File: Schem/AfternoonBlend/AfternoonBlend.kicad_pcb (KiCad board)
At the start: 4 copper layers, 160 x 64.4 mm, 67 parts, among them J1 pBITzBus, J4 STX-3120-3B, J5 Conn_01x03, SW1 SW_Coded_SH-7070, U1 74HC688, U10 LM4880MX/NOPB, U11 SN76489AN, U12 SN76489AN, U2 TLV2372, U3 AD7801BRUZ, U6 SN76489AN, U7 SN76489AN, U8 74HC138, U9 74HCT21, Y1 ECS-2100A-035

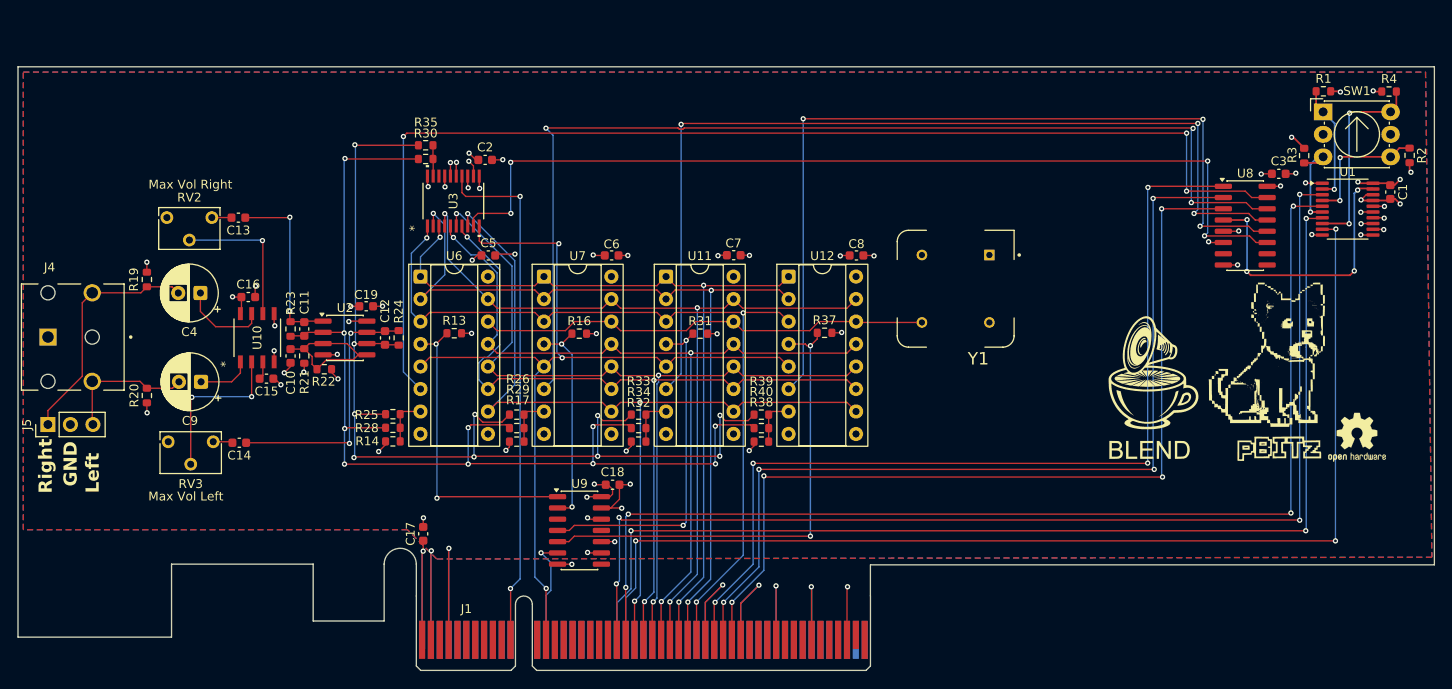
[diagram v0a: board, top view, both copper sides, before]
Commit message: Added a buffer on the Data Line to avoid overloading the CPU data bus with the 5 ICs on the board.
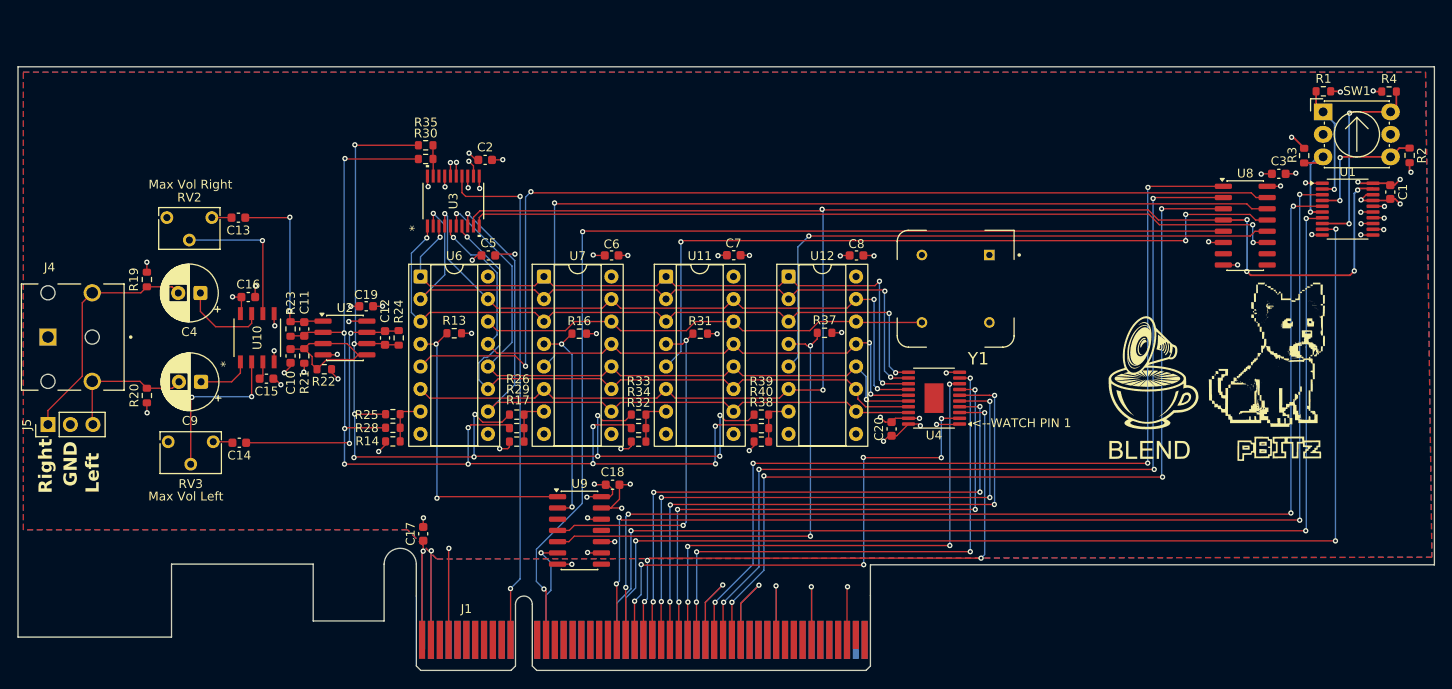
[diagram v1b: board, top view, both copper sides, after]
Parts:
- removed REF**: OSHW-Logo2_7.3x6mm_SilkScreen, Symbol:OSHW-Logo2_7.3x6mm_SilkScreen
- added C20: 100n, Capacitor_SMD:C_0603_1608Metric, F.Cu at (162.5, 104.7)
- added U4: 74HCT541, Package_SO:TSSOP-20-1EP_4.4x6.5mm_P0.65mm_EP2.15x3.35mm, F.Cu at (167.3, 101.2)
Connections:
- J1 pad B23: /Sound/D0 -> /pBITz Bus Interface/D0
- J1 pad B24: /Sound/D1 -> /pBITz Bus Interface/D1
- J1 pad B25: /Sound/D2 -> /pBITz Bus Interface/D2
- J1 pad B26: /Sound/D3 -> /pBITz Bus Interface/D3
- J1 pad B27: /Sound/D4 -> /pBITz Bus Interface/D4
- J1 pad B28: /Sound/D5 -> /pBITz Bus Interface/D5
- J1 pad B29: /Sound/D6 -> /pBITz Bus Interface/D6
- J1 pad B30: /Sound/D7 -> /pBITz Bus Interface/D7
- U11 pad 1: /Sound/D5 -> /Sound/DB5
- U11 pad 10: /Sound/D0 -> /Sound/DB0
- U11 pad 11: /Sound/D1 -> /Sound/DB1
- U11 pad 12: /Sound/D2 -> /Sound/DB2
- U11 pad 13: /Sound/D3 -> /Sound/DB3
- U11 pad 15: /Sound/D4 -> /Sound/DB4
- U11 pad 2: /Sound/D6 -> /Sound/DB6
- U11 pad 3: /Sound/D7 -> /Sound/DB7
- U11 pad 5: /Sound/~{WR} -> /Sound/~{PSG2}
- U11 pad 6: /Sound/~{PSG2} -> /Device Select Decode/~{CS_SOUND}
- U12 pad 1: /Sound/D5 -> /Sound/DB5
- U12 pad 10: /Sound/D0 -> /Sound/DB0
- U12 pad 11: /Sound/D1 -> /Sound/DB1
- U12 pad 12: /Sound/D2 -> /Sound/DB2
- U12 pad 13: /Sound/D3 -> /Sound/DB3
- U12 pad 15: /Sound/D4 -> /Sound/DB4
- U12 pad 2: /Sound/D6 -> /Sound/DB6
- U12 pad 3: /Sound/D7 -> /Sound/DB7
- U12 pad 5: /Sound/~{WR} -> /Sound/~{PSG3}
- U12 pad 6: /Sound/~{PSG3} -> /Device Select Decode/~{CS_SOUND}
- U3 pad 1: /Sound/D7 -> /Sound/DB7
- U3 pad 10: /Sound/~{WR} -> /Sound/~{PCM}
- U3 pad 2: /Sound/D6 -> /Sound/DB6
- U3 pad 3: /Sound/D5 -> /Sound/DB5
- U3 pad 4: /Sound/D4 -> /Sound/DB4
- U3 pad 5: /Sound/D3 -> /Sound/DB3
- U3 pad 6: /Sound/D2 -> /Sound/DB2
- U3 pad 7: /Sound/D1 -> /Sound/DB1
- U3 pad 8: /Sound/D0 -> /Sound/DB0
- U3 pad 9: /Sound/~{PCM} -> /Device Select Decode/~{CS_SOUND}
- U6 pad 1: /Sound/D5 -> /Sound/DB5
- U6 pad 10: /Sound/D0 -> /Sound/DB0
- U6 pad 11: /Sound/D1 -> /Sound/DB1
- U6 pad 12: /Sound/D2 -> /Sound/DB2
- U6 pad 13: /Sound/D3 -> /Sound/DB3
- U6 pad 15: /Sound/D4 -> /Sound/DB4
- U6 pad 2: /Sound/D6 -> /Sound/DB6
- U6 pad 3: /Sound/D7 -> /Sound/DB7
- U6 pad 5: /Sound/~{WR} -> /Sound/~{PSG0}
- U6 pad 6: /Sound/~{PSG0} -> /Device Select Decode/~{CS_SOUND}
- U7 pad 1: /Sound/D5 -> /Sound/DB5
- U7 pad 10: /Sound/D0 -> /Sound/DB0
- U7 pad 11: /Sound/D1 -> /Sound/DB1
- U7 pad 12: /Sound/D2 -> /Sound/DB2
- U7 pad 13: /Sound/D3 -> /Sound/DB3
- U7 pad 15: /Sound/D4 -> /Sound/DB4
- U7 pad 2: /Sound/D6 -> /Sound/DB6
- U7 pad 3: /Sound/D7 -> /Sound/DB7
- U7 pad 5: /Sound/~{WR} -> /Sound/~{PSG1}
- U7 pad 6: /Sound/~{PSG1} -> /Device Select Decode/~{CS_SOUND}
- U8 pad 5: GND -> /Sound/~{WR}
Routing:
- net /Device Select Decode/~{CS_SOUND}: track 32.2 -> 187.3 mm, vias 4 -> 6
- net /Sound/D0: track 98.5 -> 0.00 mm, vias 3 -> 0
- net /Sound/D6: track 97.5 -> 0.00 mm, vias 3 -> 0
- net /Sound/D2: track 96.9 -> 0.00 mm, vias 3 -> 0
- net /Sound/D4: track 96.0 -> 0.00 mm, vias 3 -> 0
- net /Sound/D1: track 95.9 -> 0.00 mm, vias 3 -> 0
- net /Sound/D7: track 95.2 -> 0.00 mm, vias 3 -> 0
- net /Sound/D3: track 94.5 -> 0.00 mm, vias 3 -> 0
- net /Sound/D5: track 92.0 -> 0.00 mm, vias 3 -> 0
- net /Sound/DB6: track 0.00 -> 80.0 mm, vias 0 -> 3
- net /Sound/DB0: track 0.00 -> 77.0 mm, vias 0 -> 1
- net /Sound/DB7: track 0.00 -> 76.1 mm, vias 0 -> 3
- net /Sound/DB5: track 0.00 -> 76.0 mm, vias 0 -> 3
- net /Sound/DB2: track 0.00 -> 75.8 mm, vias 0 -> 2
- net /Sound/DB1: track 0.00 -> 73.0 mm, vias 0 -> 1
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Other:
- board text added: "<--WATCH PIN 1"

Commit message: Put back /CS_SOUND as the qualifying signal instead of /WR
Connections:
- U11 pad 5: /Sound/~{PSG2} -> /Sound/~{WR}
- U11 pad 6: /Device Select Decode/~{CS_SOUND} -> /Sound/~{PSG2}
- U12 pad 5: /Sound/~{PSG3} -> /Sound/~{WR}
- U12 pad 6: /Device Select Decode/~{CS_SOUND} -> /Sound/~{PSG3}
- U3 pad 10: /Sound/~{PCM} -> /Sound/~{WR}
- U3 pad 9: /Device Select Decode/~{CS_SOUND} -> /Sound/~{PCM}
- U6 pad 5: /Sound/~{PSG0} -> /Sound/~{WR}
- U6 pad 6: /Device Select Decode/~{CS_SOUND} -> /Sound/~{PSG0}
- U7 pad 5: /Sound/~{PSG1} -> /Sound/~{WR}
- U7 pad 6: /Device Select Decode/~{CS_SOUND} -> /Sound/~{PSG1}
- U8 pad 5: /Sound/~{WR} -> GND
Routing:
- net /Device Select Decode/~{CS_SOUND}: track 187.3 -> 32.2 mm, vias 6 -> 4
- net /Sound/~{WR}: track 121.1 -> 95.0 mm
- net /Sound/~{PCM}: track 92.6 -> 95.4 mm
- net /Sound/~{PSG3}: track 67.7 -> 70.2 mm
- net /Sound/~{PSG2}: track 84.3 -> 86.8 mm
- net /Sound/~{PSG1}: track 99.7 -> 102.3 mm
- net GND: track 152.4 -> 154.0 mm, vias 52 -> 53
- net /Sound/~{PSG0}: track 116.3 -> 117.3 mm

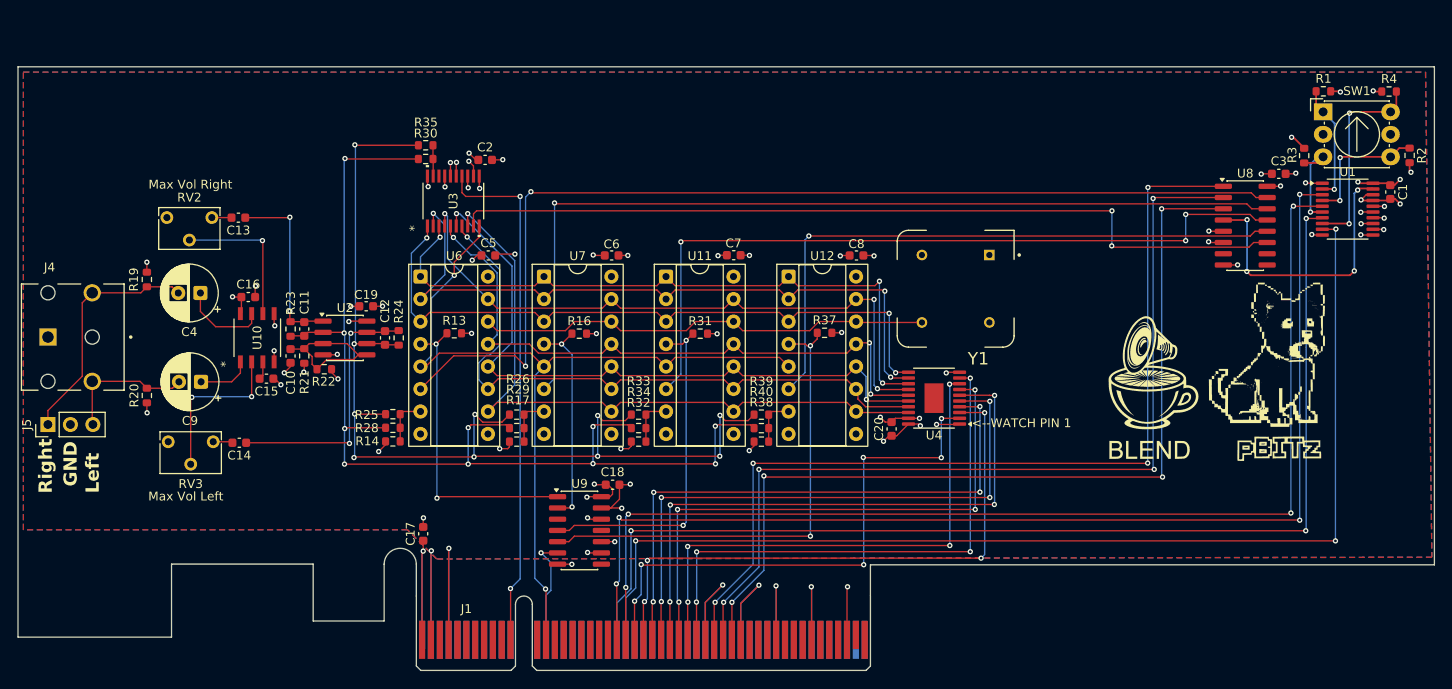
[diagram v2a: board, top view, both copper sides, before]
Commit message: Added wait-state generation to cope with a 10MHz cpu
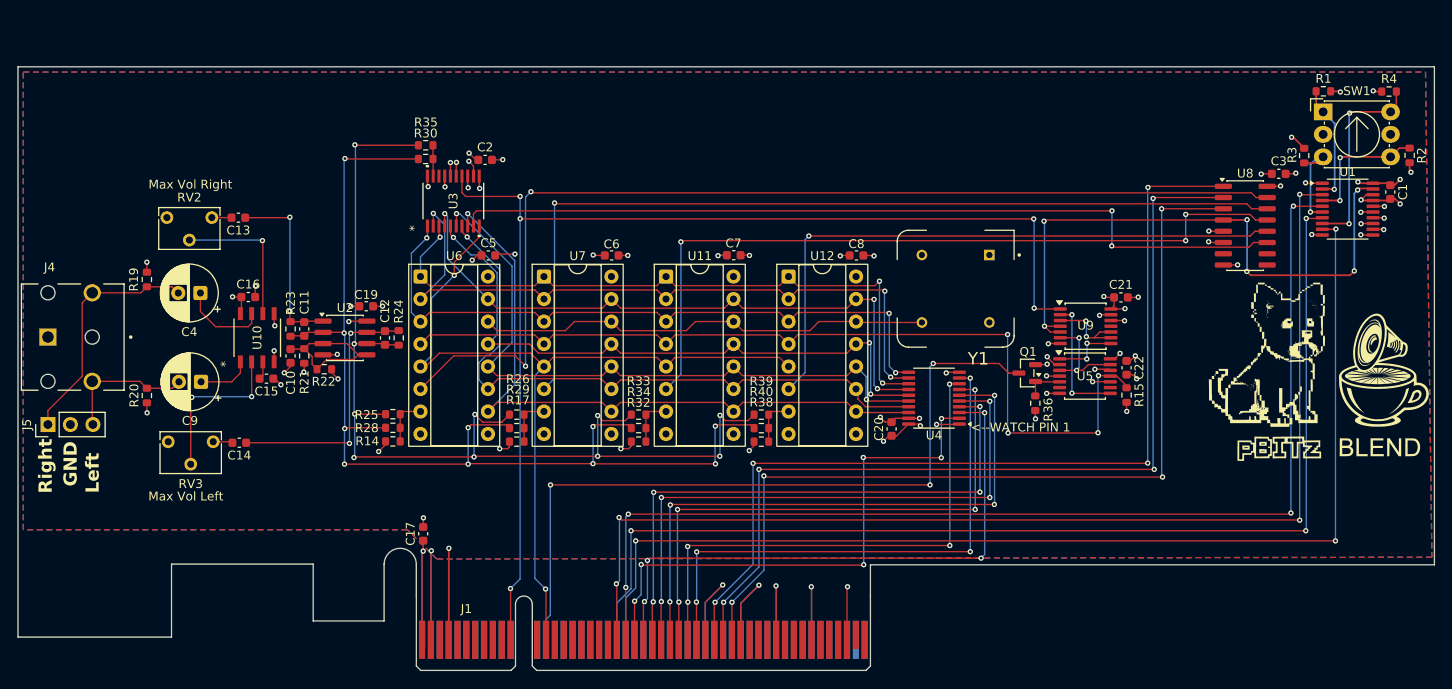
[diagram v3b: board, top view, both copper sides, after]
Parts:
- removed C18: 100n, Capacitor_SMD:C_0603_1608Metric
- removed R13, R16, R31, R37: 10k, Resistor_SMD:R_0603_1608Metric
- added C21: 100n, Capacitor_SMD:C_0603_1608Metric, F.Cu at (188.4, 89.8)
- added C22: 100n, Capacitor_SMD:C_0603_1608Metric, F.Cu at (189.0, 97.8)
- added Q1: 2N7002, Package_TO_SOT_SMD:SOT-23, F.Cu at (177.8, 98.4)
- added R15: 10k, Resistor_SMD:R_0603_1608Metric, F.Cu at (189.0, 100.9)
- added R36: 47k, Resistor_SMD:R_0603_1608Metric, F.Cu at (178.7, 101.8)
- added U5: 74AHCT74, Package_SO:TSSOP-14_4.4x5mm_P0.65mm, F.Cu at (184.3, 98.7)
- U4: footprint Package_SO:TSSOP-20-1EP_4.4x6.5mm_P0.65mm_EP2.15x3.35mm -> Package_SO:TSSOP-20_4.4x6.5mm_P0.65mm
- U9: value 74HCT21 -> 74AHCT00; footprint Package_SO:SOIC-14_3.9x8.7mm_P1.27mm -> Package_SO:TSSOP-14_4.4x5mm_P0.65mm
- moved U9 61.6 mm to (184.4, 93.1)
- moved G*** 26.0 mm to (217.6, 99.3)
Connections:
- U11 pad 4: /Sound/READY2 -> /Sound/READY_ALL
- U12 pad 4: /Sound/READY3 -> /Sound/READY_ALL
- U6 pad 4: /Sound/READY0 -> /Sound/READY_ALL
- U7 pad 4: /Sound/READY1 -> /Sound/READY_ALL
- U9 pad 1: /Sound/READY0 -> /Sound/~{RESET}
- U9 pad 10: GND -> /Sound/FF2_CLR
- U9 pad 11: (no net) -> unconnected-(U9-Pad11)
- U9 pad 2: /Sound/READY1 -> /Sound/~{FF2_Q}
- U9 pad 3: (no net) -> /Sound/FF2_CLR
- U9 pad 4: /Sound/READY2 -> /Device Select Decode/~{CS_SOUND}
- U9 pad 5: /Sound/READY3 -> /Device Select Decode/~{CS_SOUND}
- U9 pad 6: /Sound/~{WAIT} -> /Sound/CS_SOUND
- U9 pad 8: unconnected-(U9-Pad8) -> /Sound/~{FF2_CLR}
- U9 pad 9: GND -> /Sound/FF2_CLR
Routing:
- net /Sound/READY_ALL: track 0.00 -> 101.0 mm, vias 0 -> 4
- net /Sound/~{WAIT}: track 12.4 -> 84.6 mm, vias 1 -> 3
- net /Sound/~{RESET}: track 59.2 -> 130.3 mm, vias 2 -> 5
- net /Sound/READY3: track 54.7 -> 0.00 mm, vias 2 -> 0
- net /Sound/READY2: track 39.0 -> 0.00 mm, vias 2 -> 0
- net /Device Select Decode/~{CS_SOUND}: track 32.2 -> 68.3 mm, vias 4 -> 6
- net /Sound/READY0: track 34.6 -> 0.00 mm, vias 2 -> 0
- net /Sound/READY1: track 24.2 -> 0.00 mm, vias 2 -> 0
- net /Sound/~{FF2_Q}: track 0.00 -> 14.5 mm, vias 0 -> 2
- net /Sound/CS_SOUND: track 0.00 -> 11.9 mm, vias 0 -> 2
- net /Sound/FF2_CLR: track 0.00 -> 9.70 mm, vias 0 -> 2
- net /Sound/~{FF2_CLR}: track 0.00 -> 7.58 mm, vias 0 -> 2
- net +5V: track 90.2 -> 94.8 mm, vias 31 -> 34
- net /Sound/WAIT_GATE: track 0.00 -> 4.39 mm
- net GND: track 154.0 -> 151.6 mm, vias 53 -> 55

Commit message: Added WS Generator to sound card to match the speed of the CPU to the speed of the SN7 chips
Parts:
- added C23: 100n, Capacitor_SMD:C_0603_1608Metric, F.Cu at (202.2, 90.0)
- added U14: 74AHC20, Package_SO:TSSOP-14_4.4x5mm_P0.65mm, F.Cu at (198.1, 93.3)
- R15: value 10k -> 2k2
- moved G*** 2.18 mm to (208.4, 96.9)
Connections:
- U8 pad 5: GND -> /Sound/~{WR}
- U9 pad 4: /Device Select Decode/~{CS_SOUND} -> GND
- U9 pad 5: /Device Select Decode/~{CS_SOUND} -> GND
- U9 pad 6: /Sound/CS_SOUND -> unconnected-(U9-Pad6)
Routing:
- net /Sound/~{WR}: track 95.0 -> 158.8 mm, vias 2 -> 4
- net /Device Select Decode/~{CS_SOUND}: track 68.3 -> 32.2 mm, vias 6 -> 4
- net /Sound/~{PSG0}: track 117.3 -> 133.0 mm, vias 2 -> 4
- net /Sound/~{PSG1}: track 102.3 -> 116.2 mm, vias 1 -> 3
- net /Sound/~{PSG3}: track 70.2 -> 83.1 mm, vias 1 -> 3
- net /Sound/~{PSG2}: track 86.8 -> 98.4 mm, vias 3 -> 4
- net GND: track 151.6 -> 161.1 mm, vias 55 -> 62
- net +5V: track 94.8 -> 100.2 mm, vias 34 -> 36
- net /Sound/CS_SOUND: track 11.9 -> 17.3 mm

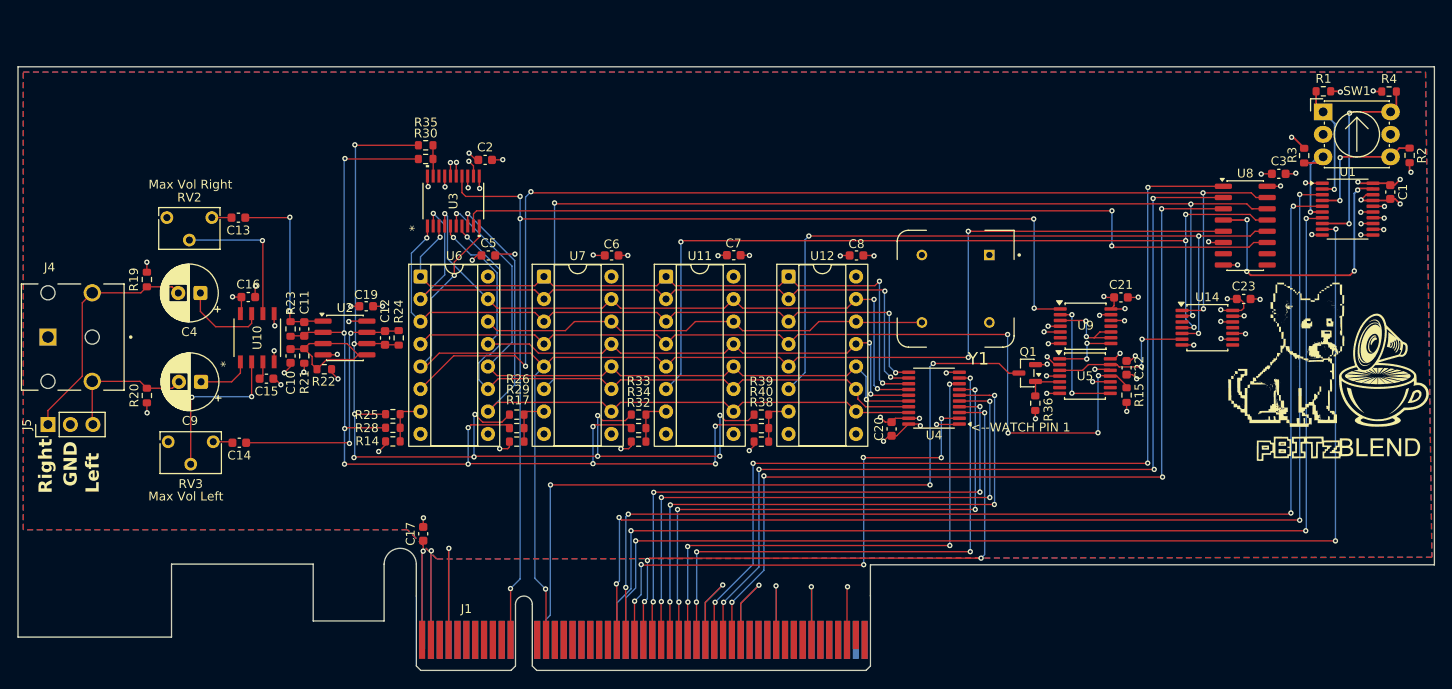
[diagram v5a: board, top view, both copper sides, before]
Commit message: Moved to the DIN Connector
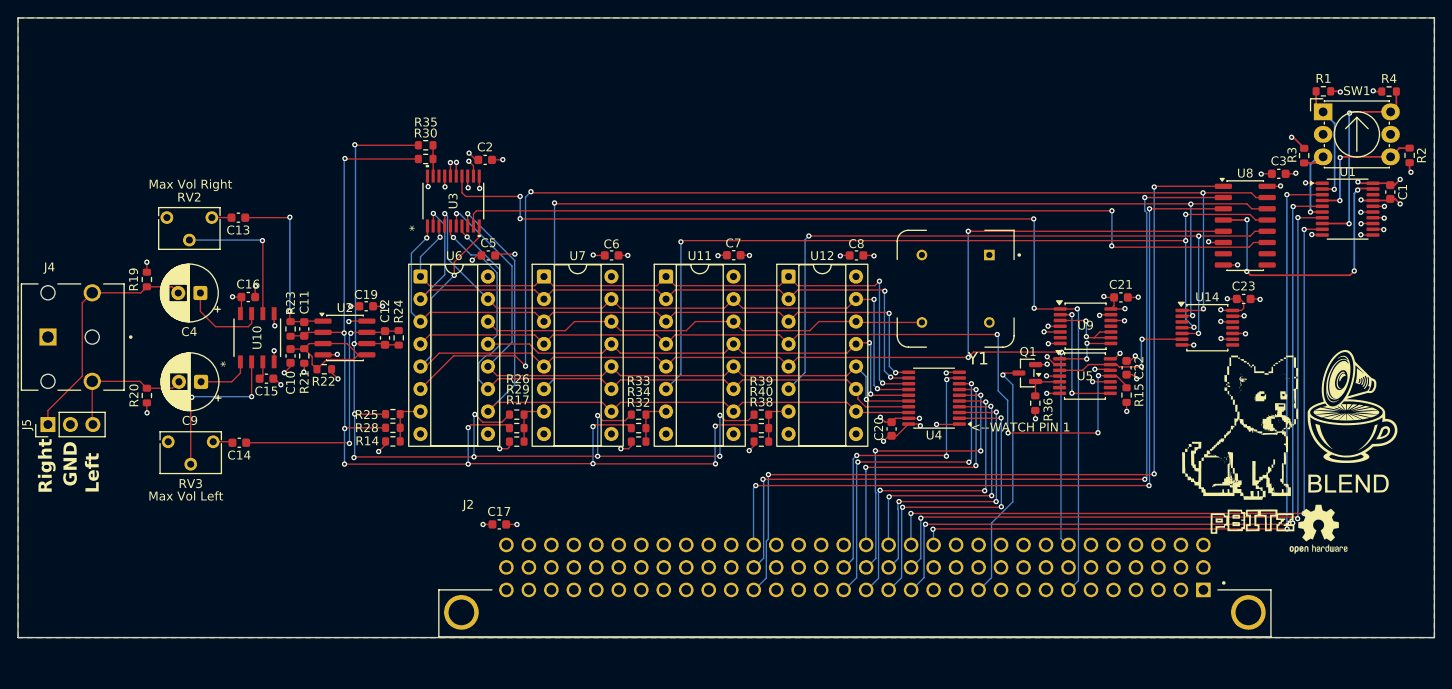
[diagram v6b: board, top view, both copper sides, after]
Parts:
- removed J1: pBITzBus, Connector_PCBEdge:BUS_PCIexpress_x8
- added J2: ~, Footprints:AMPHENOL_86093967113T55F1LF, F.Cu at (158.3, 125.4)
- added REF**: OSHW-Logo2_7.3x6mm_SilkScreen, Symbol:OSHW-Logo2_7.3x6mm_SilkScreen, F.Cu at (210.7, 116.0)
- U14: value 74AHC20 -> 74HC20
- U8: value 74HC138 -> 74AHCT138
- moved G*** 9.75 mm to (203.2, 105.1)
- moved C17 8.66 mm to (118.1, 115.5), turned to 0 degrees
- moved G*** 5.42 mm to (214.0, 103.4)
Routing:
- net GND: track 161.1 -> 80.7 mm, vias 62 -> 56
- net /Sound/~{WAIT}: track 84.6 -> 28.4 mm, vias 3 -> 1
- net /Device Select Decode/CS0: track 130.4 -> 83.7 mm, vias 4 -> 3
- net /Device Select Decode/CS3: track 127.5 -> 82.2 mm
- net /Device Select Decode/CS2: track 126.4 -> 85.6 mm
- net +5V: track 100.2 -> 60.3 mm, vias 36 -> 35
- net /Device Select Decode/CS1: track 127.3 -> 88.8 mm, vias 4 -> 3
- net /pBITz Bus Interface/D2: track 65.6 -> 30.9 mm, vias 4 -> 3
- net /pBITz Bus Interface/D4: track 68.2 -> 34.4 mm, vias 4 -> 3
- net /pBITz Bus Interface/D1: track 66.4 -> 33.4 mm, vias 4 -> 3
- net /pBITz Bus Interface/D5: track 63.7 -> 31.9 mm, vias 4 -> 3
- net /pBITz Bus Interface/D3: track 67.5 -> 37.0 mm, vias 4 -> 3
- net /pBITz Bus Interface/D7: track 61.7 -> 33.7 mm, vias 4 -> 3
- net /pBITz Bus Interface/D0: track 61.5 -> 36.1 mm, vias 6 -> 3
- net /pBITz Bus Interface/D6: track 59.6 -> 38.1 mm, vias 4 -> 3
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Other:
- board size 160 x 64.4 mm -> 160 x 70 mm
